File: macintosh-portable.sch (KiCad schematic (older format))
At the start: 0 parts

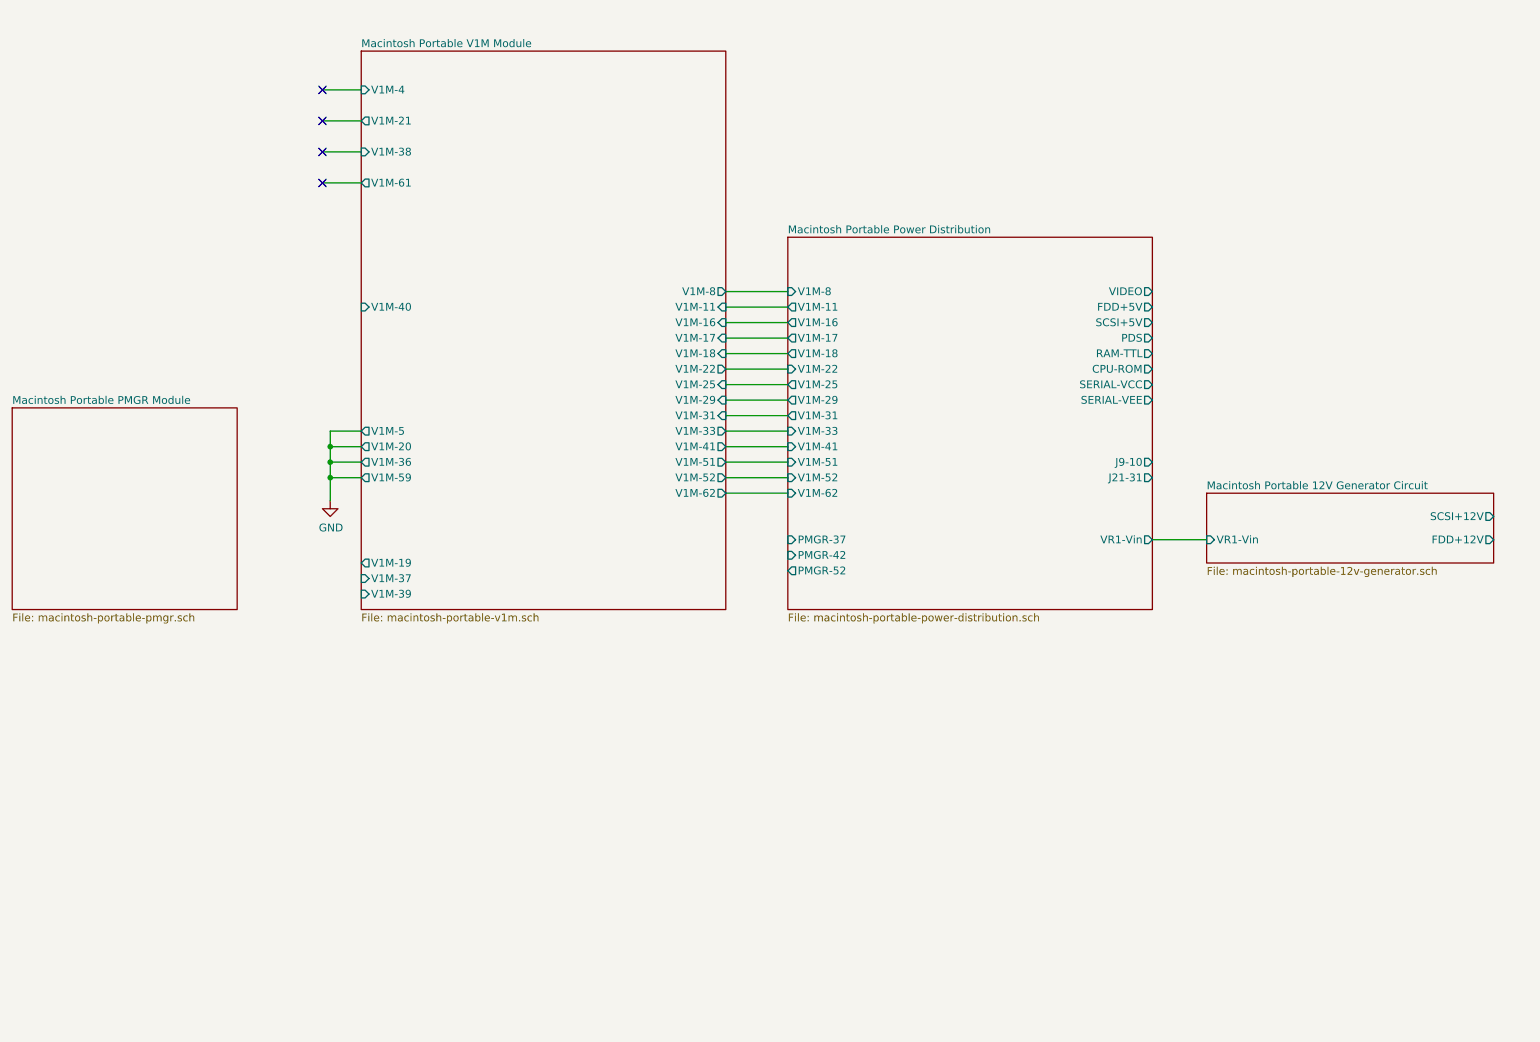
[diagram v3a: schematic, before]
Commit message: Progress on PMGR chip
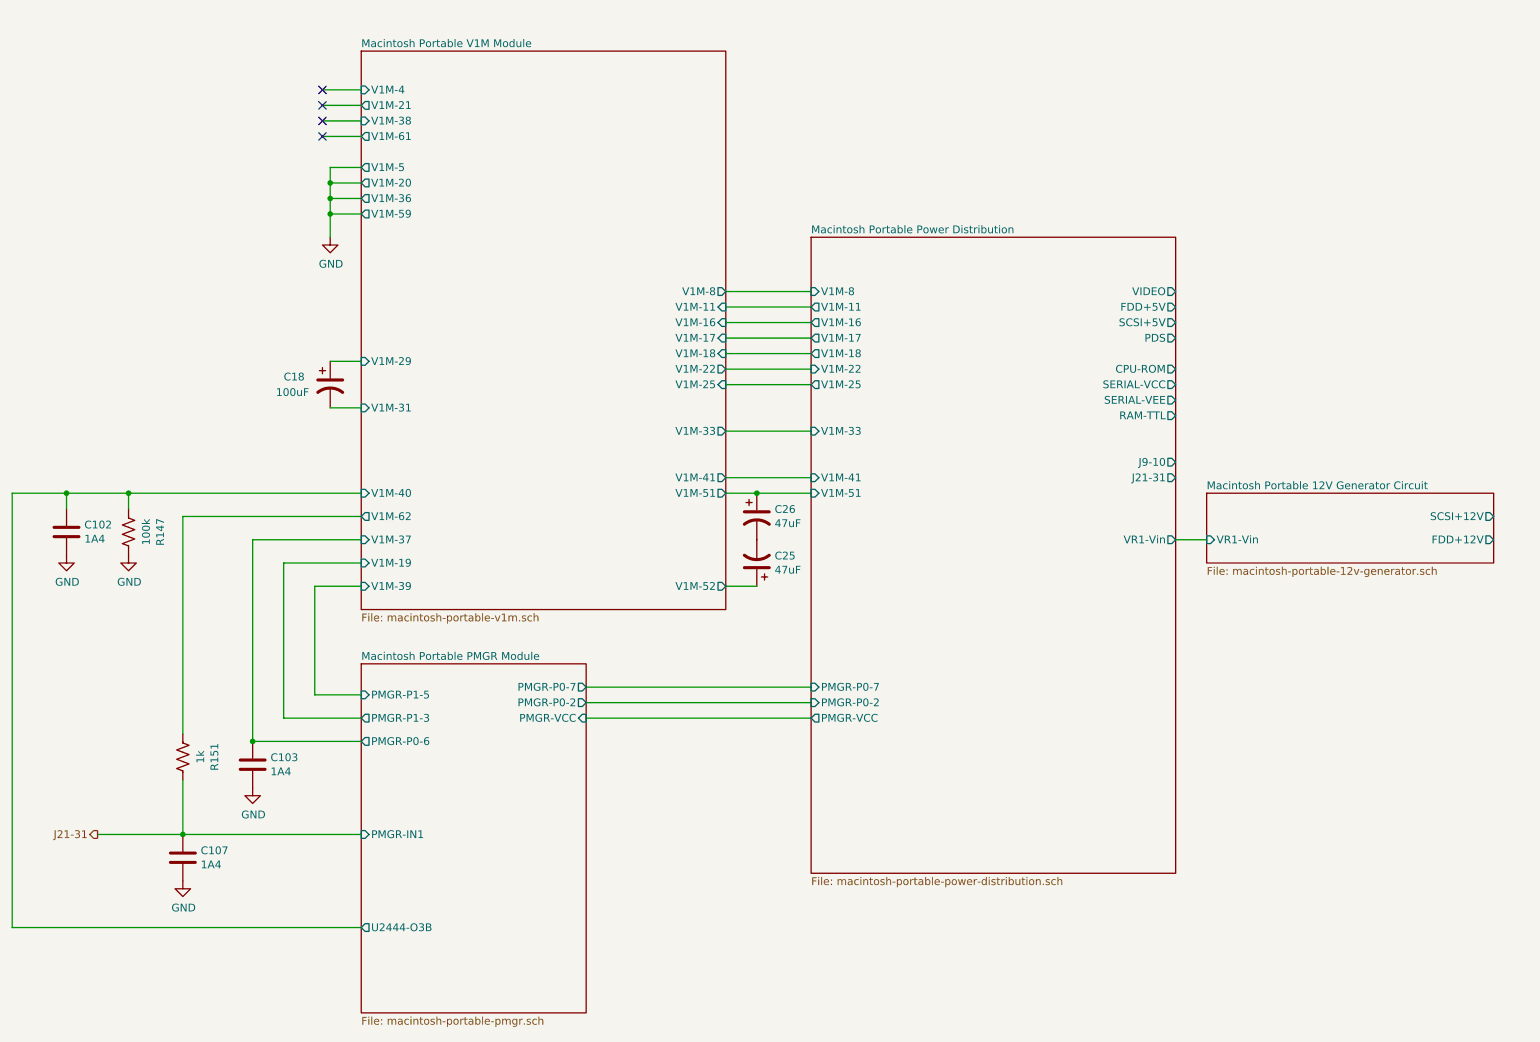
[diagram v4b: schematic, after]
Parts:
- added C102, C103, C107: 1A4, symbol Device:C
- added C18: 100uF, symbol Device:CP1
- added C25, C26: 47uF, symbol Device:CP1
- added R147: 100k, symbol Device:R_US
- added R151: 1k, symbol Device:R_US
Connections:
- net GND: now also C102.2, C103.2, C107.2, R147.1
- net Macintosh Portable Power Distribution/V1M-51: now also C26.1
- new net: C25.2, C26.2
- new net J21-31: C107.1, R151.1
- new net Macintosh Portable PMGR Module/PMGR-P0-6: C103.1
- new net Macintosh Portable PMGR Module/U2444-O3B: C102.1, R147.2
- new net Macintosh Portable V1M Module/V1M-29: C18.1
- new net Macintosh Portable V1M Module/V1M-31: C18.2
- new net Macintosh Portable V1M Module/V1M-52: C25.1
- new net Macintosh Portable V1M Module/V1M-62: R151.2

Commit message: Added reset circuit.
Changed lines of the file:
@@
 Sheet 1 5
 Title "Macintosh Portable Power"
-Date "2019-06-08"
-Rev "0.13"
+Date "2019-06-12"
+Rev "0.14"
 Comp "https://oldcrap.org"
 Comment1 "Author: Pawel Pieczul"
@@
 F7 "V1M-8" I L 6200 2600 50
 F8 "FDD+5V" O R 8550 2700 50
-F9 "CPU-ROM" O R 8550 3100 50
+F9 "CPU-ROM-VCC" O L 6200 5450 50
 F10 "PDS" O R 8550 2900 50
 F11 "VIDEO" O R 8550 2600 50
@@
 F0 "Macintosh Portable PMGR Module" 50
 F1 "macintosh-portable-pmgr.sch" 50
-F2 "PMGR-P1-3" O L 3300 5350 50
+F2 "PMGR-P1-3" I L 3300 5350 50
 F3 "PMGR-P0-7" O R 4750 5150 50
 F4 "PMGR-P0-2" O R 4750 5250 50
@@
 F8 "U2444-O3B" O L 3300 6700 50
 F9 "PMGR-P1-5" I L 3300 5200 50
+F10 "RESET" O R 4750 7000 50
+F11 "MISC-GLU-6" O R 4750 6900 50
+F12 "HALT" O R 4750 7100 50
+F13 "CPU-ROM-VCC" I R 4750 5450 50
 $EndSheet
+Wire Wire Line
+	4750 5450 6200 5450
 $EndSCHEMATC

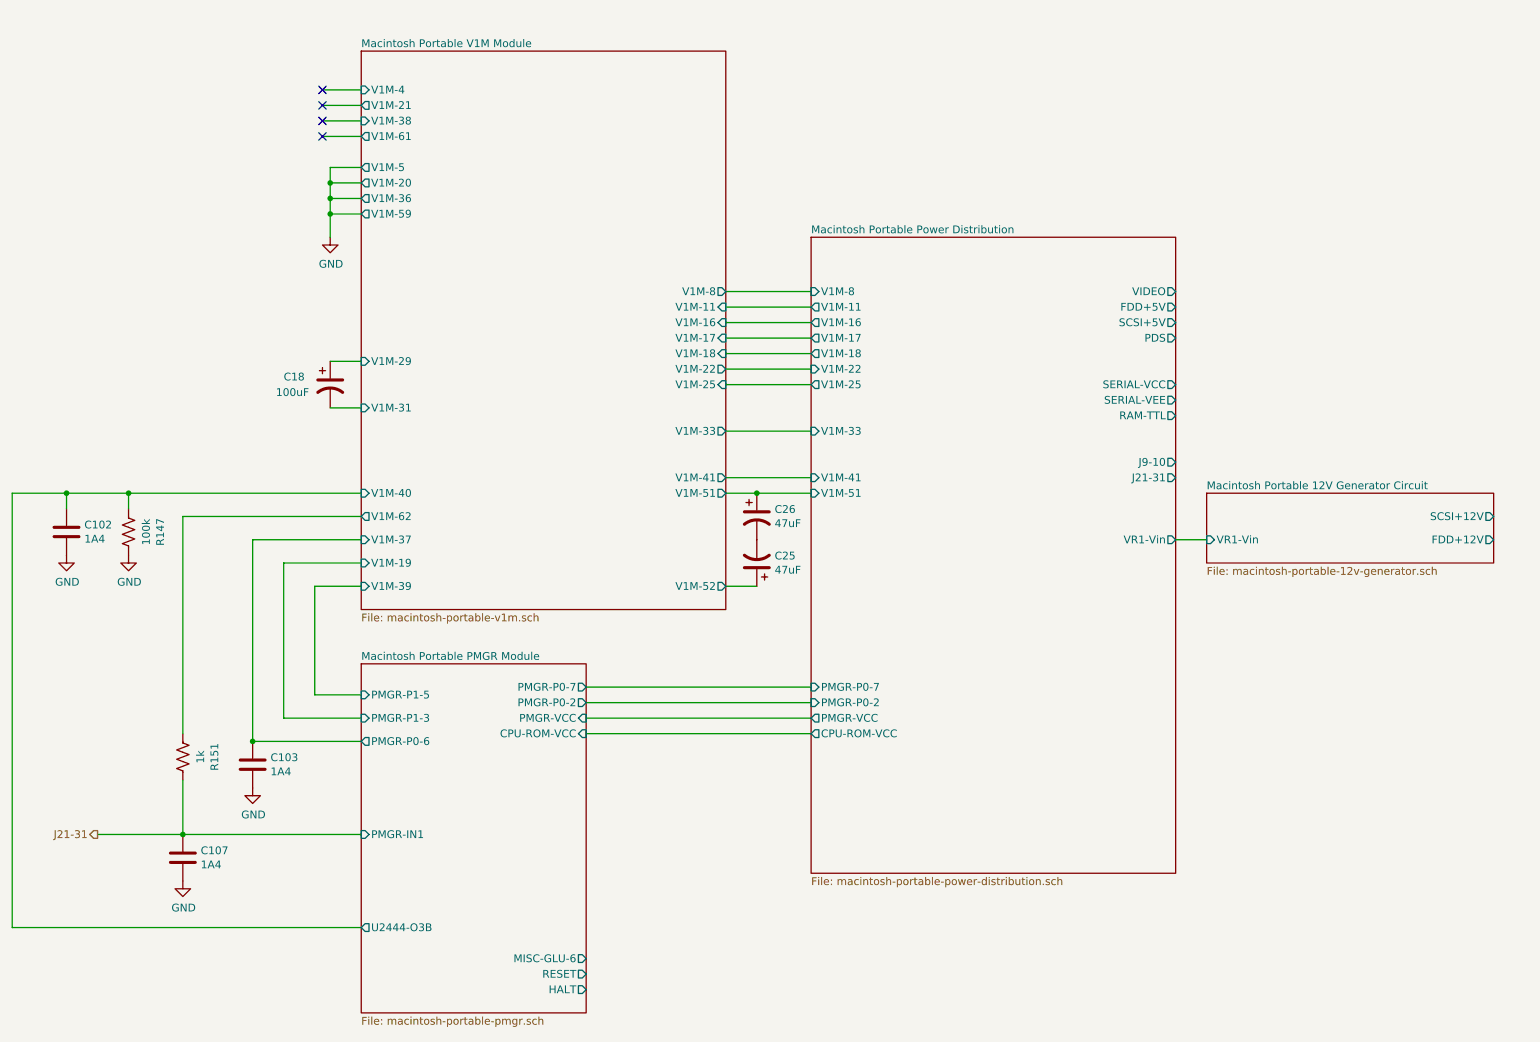
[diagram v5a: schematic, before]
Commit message: More progress on PMGR chip
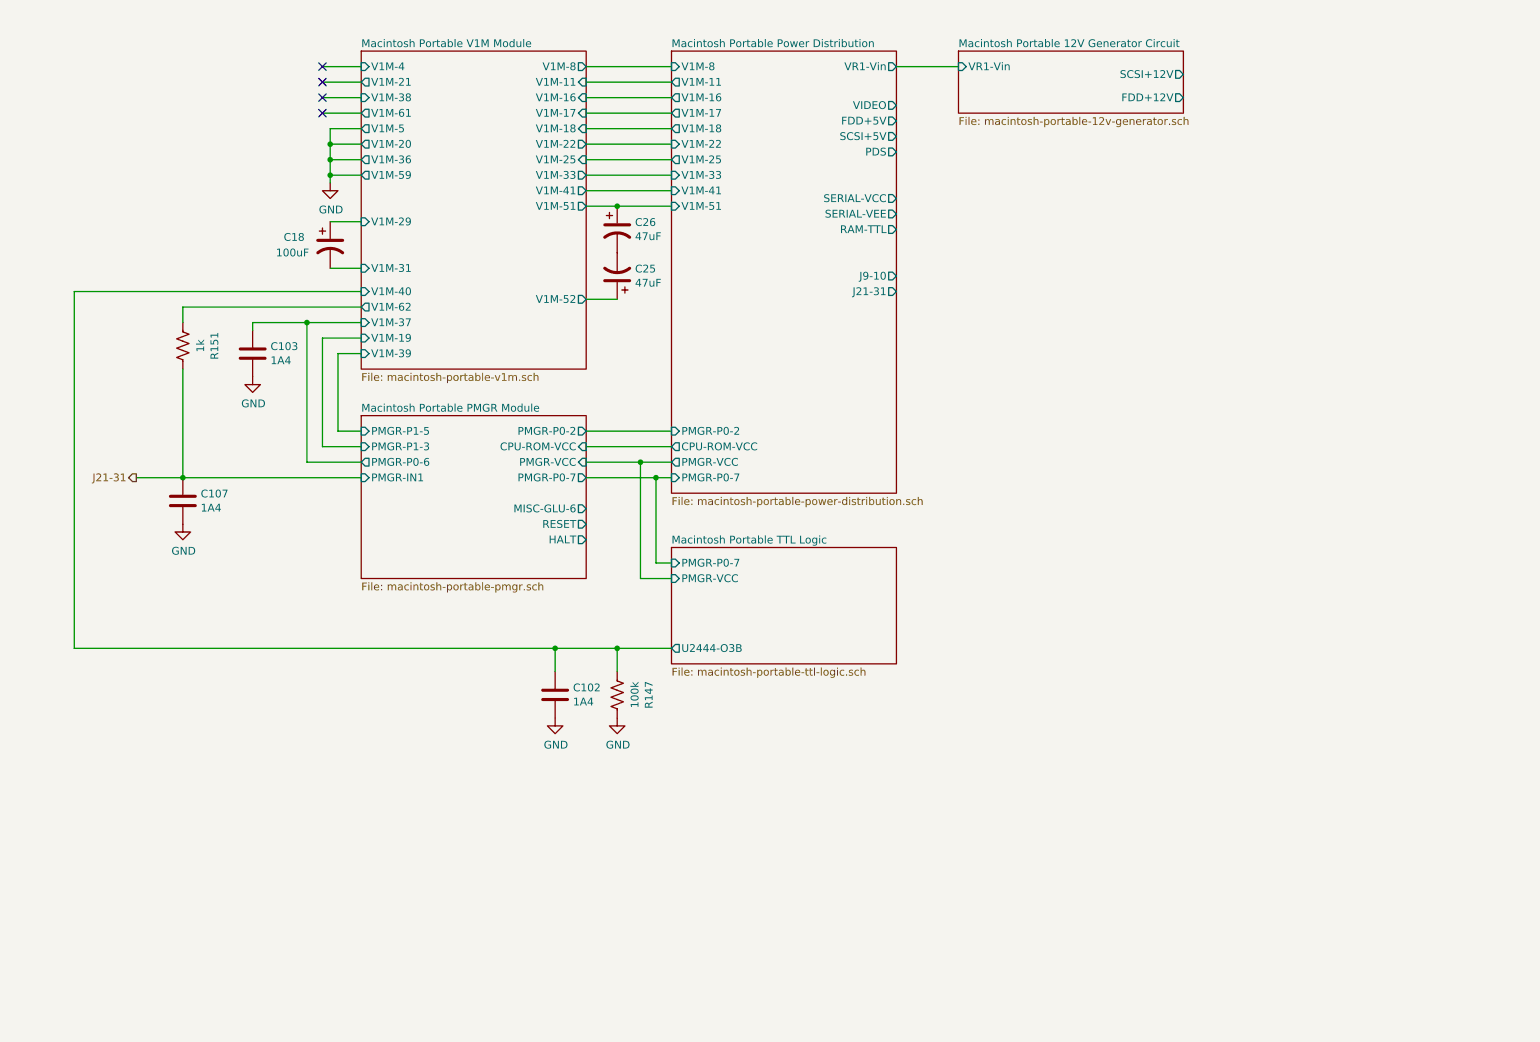
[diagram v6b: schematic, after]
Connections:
- net Macintosh Portable PMGR Module/U2444-O3B renamed Macintosh Portable TTL Logic/U2444-O3B
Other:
- moved on the sheet: C102, C103, C107, C18, C25, C26, R147, R151
